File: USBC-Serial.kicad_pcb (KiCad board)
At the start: 2 copper layers, 19.5 x 29.2 mm, 10 parts, among them J1 USB_C_Receptacle_USB2.0_16P, J2 Conn_01x06_Pin, U1 CH343P

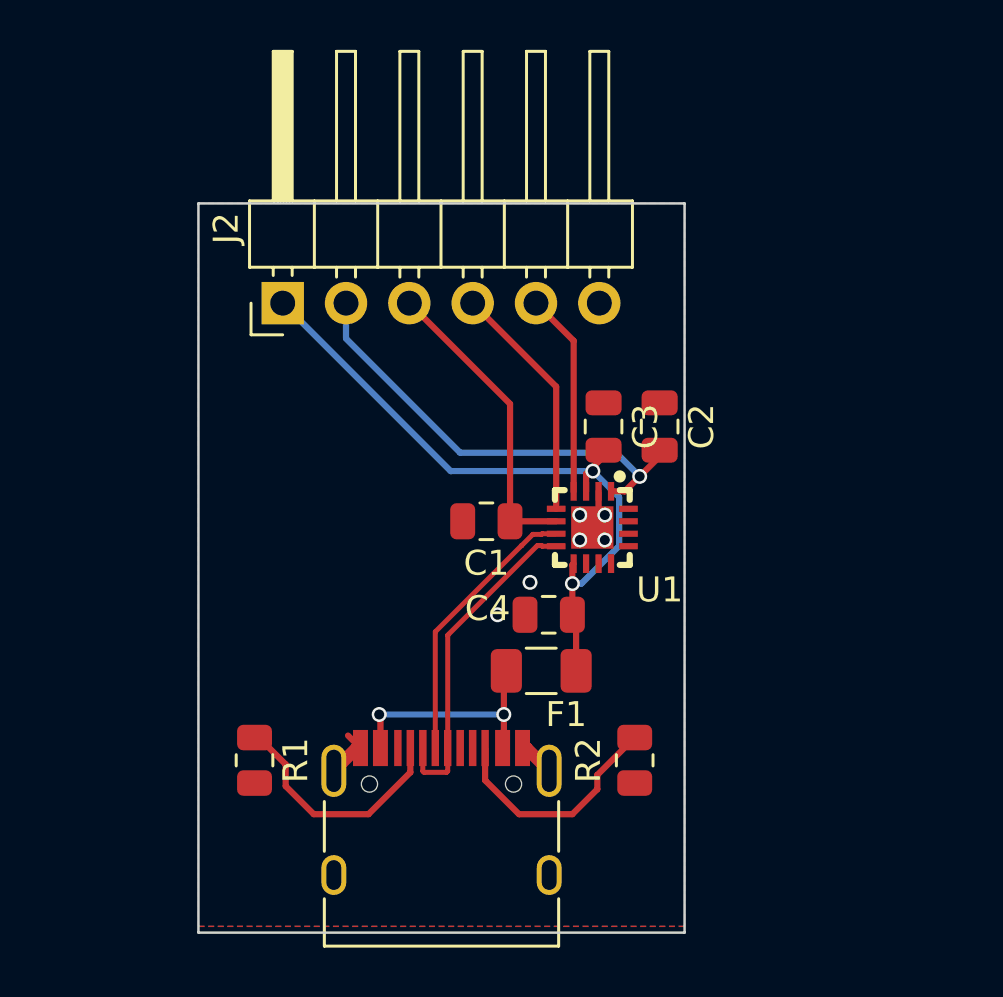
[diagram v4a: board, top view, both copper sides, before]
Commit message: move J2 to the left, conserve some more space
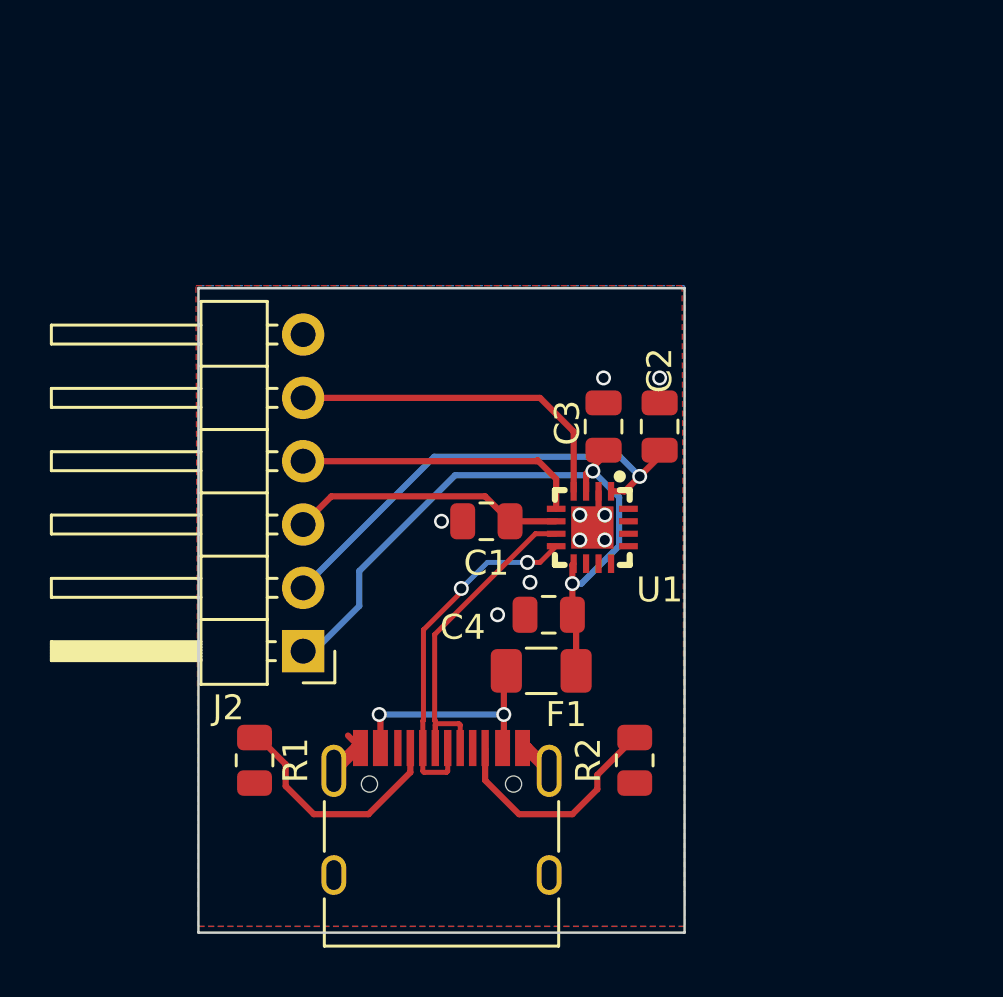
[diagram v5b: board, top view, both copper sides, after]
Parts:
- moved J2 14.0 mm to (17.2, 31.0), turned to 180 degrees
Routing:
- net /TXD: track 8.18 -> 13.8 mm
- net /D+: track 11.1 -> 14.3 mm
- net /RXD: track 9.99 -> 11.7 mm
- net /D-: track 13.3 -> 14.8 mm, vias 0 -> 2
- net +3.3V: track 12.3 -> 11.0 mm
- net /VIO: track 18.0 -> 18.5 mm
- net GND: vias 6 -> 9
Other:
- board size 19.5 x 29.2 mm -> 19.5 x 25.9 mm

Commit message: add text, delete old gerber files
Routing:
- net GND: track 5.62 -> 4.91 mm
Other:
- board text added: "3.3V"
- board text added: "5V"
- board text added: "GND"
- board text added: "RX"
- board text added: "TX"
- board text added: "VIO"
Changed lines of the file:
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@@
     (property "ki_keywords" "cap capacitor")
     (attr smd)
-    (fp_text reference "C2" (at -2.25 0 90) (layer "F.SilkS")
+    (fp_text reference "C2" (at 2.55 -0.25 90) (layer "F.SilkS")
         (effects (font (size 1 1) (thickness 0.15)))
     )
@@
   (gr_rect (start 13 16.4) (end 32.5 42.25)
     (stroke (width 0.1) (type default)) (fill none) (layer "Edge.Cuts"))
+  (gr_text "GND" (at 19 19) (layer "F.SilkS")
+    (effects (font (size 1 1) (thickness 0.15)) (justify left bottom))
+  )
+  (gr_text "3.3V" (at 19 26.5) (layer "F.SilkS")
+    (effects (font (size 1 1) (thickness 0.15)) (justify left bottom))
+  )
+  (gr_text "5V" (at 19 31.75) (layer "F.SilkS")
+    (effects (font (size 1 1) (thickness 0.15)) (justify left bottom))
+  )
+  (gr_text "RX" (at 19 24) (layer "F.SilkS")
+    (effects (font (size 1 1) (thickness 0.15)) (justify left bottom))
+  )
+  (gr_text "TX" (at 19 21.5) (layer "F.SilkS")
+    (effects (font (size 1 1) (thickness 0.15)) (justify left bottom))
+  )
+  (gr_text "VIO" (at 19 29.25) (layer "F.SilkS")
+    (effects (font (size 1 1) (thickness 0.15)) (justify left bottom))
+  )
   (segment (start 27.35 25.75) (end 25.5 25.75) (width 0.25) (layer "F.Cu") (net 1))
-  (segment (start 17.2 25.88) (end 18.33 24.75) (width 0.25) (layer "F.Cu") (net 1))
-  (segment (start 24.5 24.75) (end 25.5 25.75) (width 0.25) (layer "F.Cu") (net 1))
-  (segment (start 18.33 24.75) (end 24.5 24.75) (width 0.25) (layer "F.Cu") (net 1))
+  (segment (start 24 24.25) (end 25.5 25.75) (width 0.25) (layer "F.Cu") (net 1))
+  (segment (start 18.83 24.25) (end 24 24.25) (width 0.25) (layer "F.Cu") (net 1))
+  (segment (start 17.2 25.88) (end 18.83 24.25) (width 0.25) (layer "F.Cu") (net 1))
   (segment (start 26.075 34.770483) (end 26 34.845483) (width 0.25) (layer "F.Cu") (net 2))
   (segment (start 26.155 34.845483) (end 27.07 35.760483) (width 0.5) (layer "F.Cu") (net 2))
@@
   (segment (start 29.3 25.5) (end 29.05 25.75) (width 0.25) (layer "F.Cu") (net 2))
   (segment (start 19.5 34.845483) (end 19.345 34.845483) (width 0.5) (layer "F.Cu") (net 2))
-  (segment (start 19 34.345483) (end 19.5 34.845483) (width 0.25) (layer "F.Cu") (net 2))
   (segment (start 19.345 34.845483) (end 18.43 35.760483) (width 0.5) (layer "F.Cu") (net 2))
   (via (at 28.3 25.5) (size 0.6) (drill 0.4) (layers "F.Cu" "B.Cu") (net 2))
@@
   (segment (start 22.025 30.1068) (end 23.5909 28.5409) (width 0.2) (layer "F.Cu") (net 8))
   (segment (start 22 33.757982) (end 22.025 33.732982) (width 0.2) (layer "F.Cu") (net 8))
-  (segment (start 26.2 27.4) (end 26.7 27.4) (width 0.2) (layer "F.Cu") (net 8))
   (segment (start 27.1 26.75) (end 27.075 26.725) (width 0.2) (layer "F.Cu") (net 8))
   (segment (start 23.5909 28.4909) (end 23.545191 28.445191) (width 0.2) (layer "F.Cu") (net 8))
@@
   (segment (start 22.95 35.820483) (end 23 35.770483) (width 0.2) (layer "F.Cu") (net 8))
   (segment (start 27.35 26.75) (end 27.1 26.75) (width 0.2) (layer "F.Cu") (net 8))
+  (segment (start 26.75 27.25) (end 26.85 27.25) (width 0.2) (layer "F.Cu") (net 8))
   (segment (start 23.5909 28.5409) (end 23.5909 28.4909) (width 0.2) (layer "F.Cu") (net 8))
   (segment (start 23 35.770483) (end 23 34.845483) (width 0.2) (layer "F.Cu") (net 8))
+  (segment (start 26.85 27.25) (end 27.35 26.75) (width 0.2) (layer "F.Cu") (net 8))
   (segment (start 22 35.770483) (end 22.05 35.820483) (width 0.2) (layer "F.Cu") (net 8))
-  (segment (start 26.7 27.4) (end 27.35 26.75) (width 0.2) (layer "F.Cu") (net 8))
-  (via (at 26.2 27.4) (size 0.6) (drill 0.4) (layers "F.Cu" "B.Cu") (net 8))
+  (via (at 26.75 27.25) (size 0.6) (drill 0.4) (layers "F.Cu" "B.Cu") (net 8))
   (via (at 23.545191 28.445191) (size 0.6) (drill 0.4) (layers "F.Cu" "B.Cu") (net 8))
-  (segment (start 24.590382 27.4) (end 26.2 27.4) (width 0.2) (layer "B.Cu") (net 8))
-  (segment (start 23.545191 28.445191) (end 24.590382 27.4) (width 0.2) (layer "B.Cu") (net 8))
+  (segment (start 24.740382 27.25) (end 23.545191 28.445191) (width 0.2) (layer "B.Cu") (net 8))
+  (segment (start 26.75 27.25) (end 24.740382 27.25) (width 0.2) (layer "B.Cu") (net 8))
   (segment (start 28 37.5) (end 29 36.5) (width 0.25) (layer "F.Cu") (net 10))
   (segment (start 29 36.5) (end 29 35.925) (width 0.25) (layer "F.Cu") (net 10))

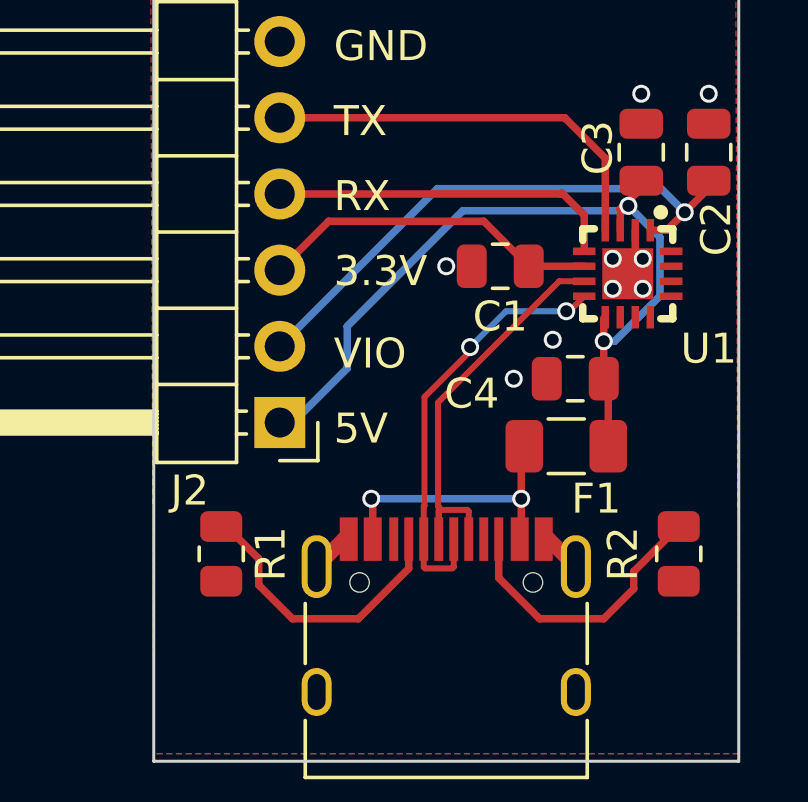
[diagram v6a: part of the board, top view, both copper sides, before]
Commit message: raret R1 and R2
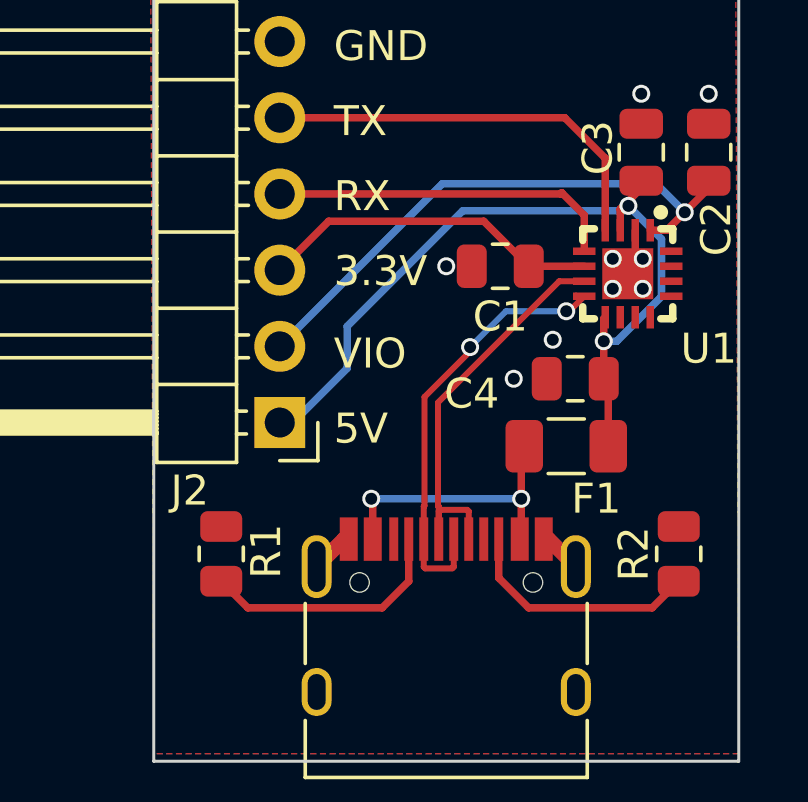
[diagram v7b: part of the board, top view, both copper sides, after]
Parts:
- turned R1 to 90 degrees
- turned R2 to 90 degrees
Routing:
- net Net-(J1-CC2): track 9.47 -> 8.07 mm
- net Net-(J1-CC1): track 9.71 -> 8.39 mm
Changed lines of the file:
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@@
   )
   (footprint "Resistor_SMD:R_0805_2012Metric" (layer "F.Cu")
-    (at 15.25 35.3375 -90)
+    (at 15.25 35.3375 90)
     (descr "Resistor SMD 0805 (2012 Metric), square (rectangular) end terminal, IPC_7351 nominal, (Body size source: IPC-SM-782 page 72, https://www.pcb-3d.com/wordpress/wp-content/uploads/ipc-sm-782a_amendment_1_and_2.pdf), generated with kicad-footprint-generator")
     (tags "resistor")
@@
     (property "ki_keywords" "R res resistor")
     (attr smd)
-    (fp_text reference "R1" (at 0 -1.65 -270) (layer "F.SilkS")
-        (effects (font (size 1 1) (thickness 0.15)))
-    )
-    (fp_text value "5.1k" (at 0.1625 1.75 -270) (layer "F.Fab") hide
-        (effects (font (size 1 1) (thickness 0.15)))
-    )
-    (fp_text user "${REFERENCE}" (at 0 0 -270) (layer "F.Fab")
+    (fp_text reference "R1" (at 0.0875 1.5 90) (layer "F.SilkS")
+        (effects (font (size 1 1) (thickness 0.15)))
+    )
+    (fp_text value "5.1k" (at 0.1625 1.75 90) (layer "F.Fab") hide
+        (effects (font (size 1 1) (thickness 0.15)))
+    )
+    (fp_text user "${REFERENCE}" (at 0 0 90) (layer "F.Fab")
         (effects (font (size 0.5 0.5) (thickness 0.08)))
     )
@@
     (fp_line (start 1 0.625) (end -1 0.625)
       (stroke (width 0.1) (type solid)) (layer "F.Fab"))
-    (pad "1" smd roundrect (at -0.9125 0 270) (size 1.025 1.4) (layers "F.Cu" "F.Paste" "F.Mask") (roundrect_rratio 0.243902439)
+    (pad "1" smd roundrect (at -0.9125 0 90) (size 1.025 1.4) (layers "F.Cu" "F.Paste" "F.Mask") (roundrect_rratio 0.243902439)
       (net 6 "Net-(J1-CC1)") (pintype "passive"))
-    (pad "2" smd roundrect (at 0.9125 0 270) (size 1.025 1.4) (layers "F.Cu" "F.Paste" "F.Mask") (roundrect_rratio 0.243902439)
+    (pad "2" smd roundrect (at 0.9125 0 90) (size 1.025 1.4) (layers "F.Cu" "F.Paste" "F.Mask") (roundrect_rratio 0.243902439)
       (net 2 "GND") (pintype "passive"))
     (model "${KICAD6_3DMODEL_DIR}/Resistor_SMD.3dshapes/R_0805_2012Metric.wrl"
@@
   )
   (footprint "Resistor_SMD:R_0805_2012Metric" (layer "F.Cu")
-    (at 30.5 35.3375 -90)
+    (at 30.5 35.3375 90)
     (descr "Resistor SMD 0805 (2012 Metric), square (rectangular) end terminal, IPC_7351 nominal, (Body size source: IPC-SM-782 page 72, https://www.pcb-3d.com/wordpress/wp-content/uploads/ipc-sm-782a_amendment_1_and_2.pdf), generated with kicad-footprint-generator")
     (tags "resistor")
@@
     (property "ki_keywords" "R res resistor")
     (attr smd)
-    (fp_text reference "R2" (at 0 1.859517 90) (layer "F.SilkS")
+    (fp_text reference "R2" (at 0 -1.5 90) (layer "F.SilkS")
         (effects (font (size 1 1) (thickness 0.15)))
     )
@@
     (fp_line (start 1 0.625) (end -1 0.625)
       (stroke (width 0.1) (type solid)) (layer "F.Fab"))
-    (pad "1" smd roundrect (at -0.9125 0 270) (size 1.025 1.4) (layers "F.Cu" "F.Paste" "F.Mask") (roundrect_rratio 0.243902439)
+    (pad "1" smd roundrect (at -0.9125 0 90) (size 1.025 1.4) (layers "F.Cu" "F.Paste" "F.Mask") (roundrect_rratio 0.243902439)
       (net 10 "Net-(J1-CC2)") (pintype "passive"))
-    (pad "2" smd roundrect (at 0.9125 0 270) (size 1.025 1.4) (layers "F.Cu" "F.Paste" "F.Mask") (roundrect_rratio 0.243902439)
+    (pad "2" smd roundrect (at 0.9125 0 90) (size 1.025 1.4) (layers "F.Cu" "F.Paste" "F.Mask") (roundrect_rratio 0.243902439)
       (net 2 "GND") (pintype "passive"))
     (model "${KICAD6_3DMODEL_DIR}/Resistor_SMD.3dshapes/R_0805_2012Metric.wrl"
@@
   (segment (start 18.83 24.25) (end 24 24.25) (width 0.25) (layer "F.Cu") (net 1))
   (segment (start 17.2 25.88) (end 18.83 24.25) (width 0.25) (layer "F.Cu") (net 1))
+  (segment (start 15.425 34.425) (end 15.25 34.425) (width 0.25) (layer "F.Cu") (net 2))
   (segment (start 26.075 34.770483) (end 26 34.845483) (width 0.25) (layer "F.Cu") (net 2))
   (segment (start 26.155 34.845483) (end 27.07 35.760483) (width 0.5) (layer "F.Cu") (net 2))
@@
   (segment (start 31.5 23.15) (end 30.1 24.55) (width 0.25) (layer "F.Cu") (net 3))
   (via (at 30.7 23.95) (size 0.6) (drill 0.4) (layers "F.Cu" "B.Cu") (net 3))
-  (segment (start 29.911961 23.161961) (end 30.7 23.95) (width 0.25) (layer "B.Cu") (net 3))
-  (segment (start 22.458039 23.161961) (end 29.911961 23.161961) (width 0.25) (layer "B.Cu") (net 3))
-  (segment (start 17.2 28.42) (end 22.458039 23.161961) (width 0.25) (layer "B.Cu") (net 3))
+  (segment (start 17.2 28.42) (end 22.62 23) (width 0.25) (layer "B.Cu") (net 3))
+  (segment (start 29.75 23) (end 30.7 23.95) (width 0.25) (layer "B.Cu") (net 3))
+  (segment (start 22.62 23) (end 29.75 23) (width 0.25) (layer "B.Cu") (net 3))
   (segment (start 28 29.5) (end 28 28.25) (width 0.25) (layer "F.Cu") (net 4))
   (segment (start 28 28.25) (end 28 27.5) (width 0.25) (layer "F.Cu") (net 4))
@@
   (via (at 28.821932 23.736961) (size 0.6) (drill 0.4) (layers "F.Cu" "B.Cu") (net 4))
   (via (at 28 28.25) (size 0.6) (drill 0.4) (layers "F.Cu" "B.Cu") (net 4))
-  (segment (start 28.363173 28.25) (end 29.875 26.738173) (width 0.25) (layer "B.Cu") (net 4))
-  (segment (start 28 28.25) (end 28.363173 28.25) (width 0.25) (layer "B.Cu") (net 4))
+  (segment (start 29.925 26.758884) (end 28.433884 28.25) (width 0.25) (layer "B.Cu") (net 4))
+  (segment (start 29.925 24.840029) (end 29.925 26.758884) (width 0.25) (layer "B.Cu") (net 4))
   (segment (start 19.45 29.15) (end 19.45 27.75) (width 0.25) (layer "B.Cu") (net 4))
-  (segment (start 29.875 26.738173) (end 29.875 24.790029) (width 0.25) (layer "B.Cu") (net 4))
   (segment (start 23.3 23.9) (end 28.658893 23.9) (width 0.25) (layer "B.Cu") (net 4))
   (segment (start 17.2 30.96) (end 17.64 30.96) (width 0.25) (layer "B.Cu") (net 4))
-  (segment (start 29.875 24.790029) (end 28.821932 23.736961) (width 0.25) (layer "B.Cu") (net 4))
+  (segment (start 28.821932 23.736961) (end 29.925 24.840029) (width 0.25) (layer "B.Cu") (net 4))
   (segment (start 28.658893 23.9) (end 28.821932 23.736961) (width 0.25) (layer "B.Cu") (net 4))
+  (segment (start 28.433884 28.25) (end 28 28.25) (width 0.25) (layer "B.Cu") (net 4))
   (segment (start 17.64 30.96) (end 19.45 29.15) (width 0.25) (layer "B.Cu") (net 4))
   (segment (start 19.45 27.75) (end 23.3 23.9) (width 0.25) (layer "B.Cu") (net 4))
@@
   (via (at 20.25 33.5) (size 0.6) (drill 0.4) (layers "F.Cu" "B.Cu") (net 5))
   (segment (start 20.25 33.5) (end 25.25 33.5) (width 0.25) (layer "B.Cu") (net 5))
-  (segment (start 17.625 37.5) (end 16.5 36.375) (width 0.25) (layer "F.Cu") (net 6))
-  (segment (start 15.425 34.425) (end 15.25 34.425) (width 0.25) (layer "F.Cu") (net 6))
-  (segment (start 21.5 35.820483) (end 19.820483 37.5) (width 0.25) (layer "F.Cu") (net 6))
-  (segment (start 16.5 35.5) (end 15.425 34.425) (width 0.25) (layer "F.Cu") (net 6))
-  (segment (start 19.820483 37.5) (end 17.625 37.5) (width 0.25) (layer "F.Cu") (net 6))
-  (segment (start 16.5 36.375) (end 16.5 35.5) (width 0.25) (layer "F.Cu") (net 6))
-  (segment (start 21.5 34.845483) (end 21.5 35.820483) (width 0.25) (layer "F.Cu") (net 6))
+  (segment (start 16.135483 37.135483) (end 20.614517 37.135483) (width 0.25) (layer "F.Cu") (net 6))
+  (segment (start 20.614517 37.135483) (end 21.5 36.25) (width 0.25) (layer "F.Cu") (net 6))
+  (segment (start 21.5 36.25) (end 21.5 34.845483) (width 0.25) (layer "F.Cu") (net 6))
+  (segment (start 15.25 36.25) (end 16.135483 37.135483) (width 0.25) (layer "F.Cu") (net 6))
   (segment (start 22.5 34.845483) (end 22.5 33.757982) (width 0.2) (layer "F.Cu") (net 7))
   (segment (start 22.475 33.732982) (end 22.475 30.2932) (width 0.2) (layer "F.Cu") (net 7))
@@
   (segment (start 24.740382 27.25) (end 23.545191 28.445191) (width 0.2) (layer "B.Cu") (net 8))
   (segment (start 26.75 27.25) (end 24.740382 27.25) (width 0.2) (layer "B.Cu") (net 8))
-  (segment (start 28 37.5) (end 29 36.5) (width 0.25) (layer "F.Cu") (net 10))
-  (segment (start 29 36.5) (end 29 35.925) (width 0.25) (layer "F.Cu") (net 10))
-  (segment (start 24.5 34.845483) (end 24.5 36.140432) (width 0.25) (layer "F.Cu") (net 10))
-  (segment (start 25.859568 37.5) (end 28 37.5) (width 0.25) (layer "F.Cu") (net 10))
-  (segment (start 24.5 36.140432) (end 25.859568 37.5) (width 0.25) (layer "F.Cu") (net 10))
-  (segment (start 29 35.925) (end 30.5 34.425) (width 0.25) (layer "F.Cu") (net 10))
+  (segment (start 30.5 36.25) (end 29.614517 37.135483) (width 0.25) (layer "F.Cu") (net 10))
+  (segment (start 24.5 36.140432) (end 24.5 34.845483) (width 0.25) (layer "F.Cu") (net 10))
+  (segment (start 25.495051 37.135483) (end 24.5 36.140432) (width 0.25) (layer "F.Cu") (net 10))
+  (segment (start 29.614517 37.135483) (end 25.495051 37.135483) (width 0.25) (layer "F.Cu") (net 10))
   (segment (start 27.35 25.25) (end 27.35 24.05) (width 0.25) (layer "F.Cu") (net 12))
   (segment (start 26.56 23.34) (end 17.2 23.34) (width 0.25) (layer "F.Cu") (net 12))
